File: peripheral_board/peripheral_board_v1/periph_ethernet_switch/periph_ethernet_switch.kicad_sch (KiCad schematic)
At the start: 57 parts, among them SW1 SW_DIP_x07, U1 KSZ9896CTXI, U2 25 MHz

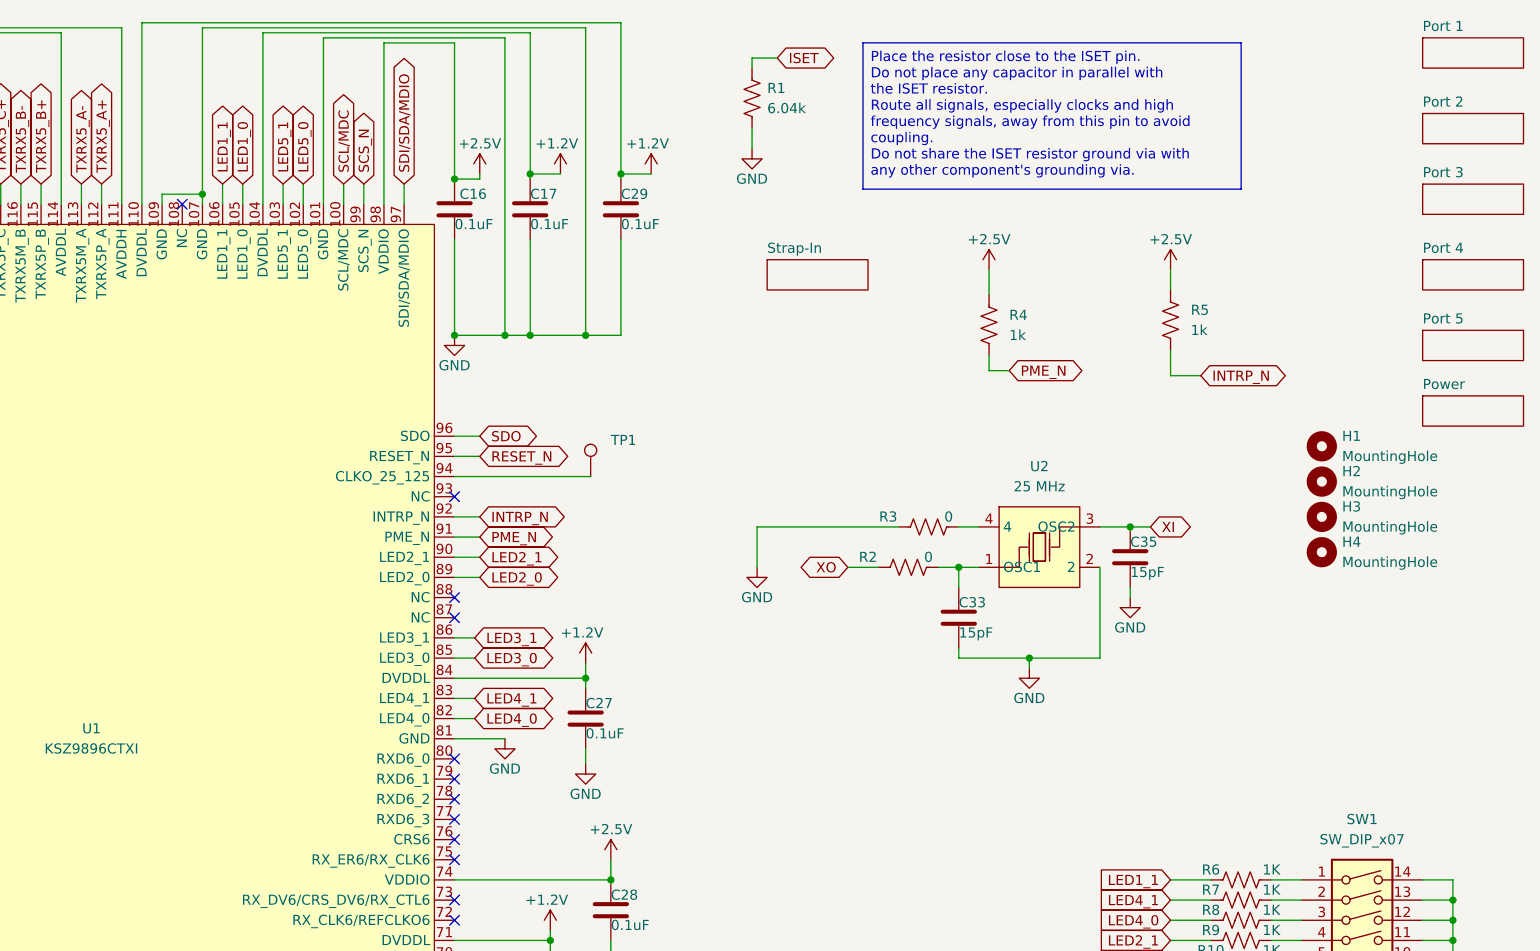
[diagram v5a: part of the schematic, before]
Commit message: Next version of the Switch
Got some feed back from Microchip. I sent it off for them look at. Will continue to make changes and updates here
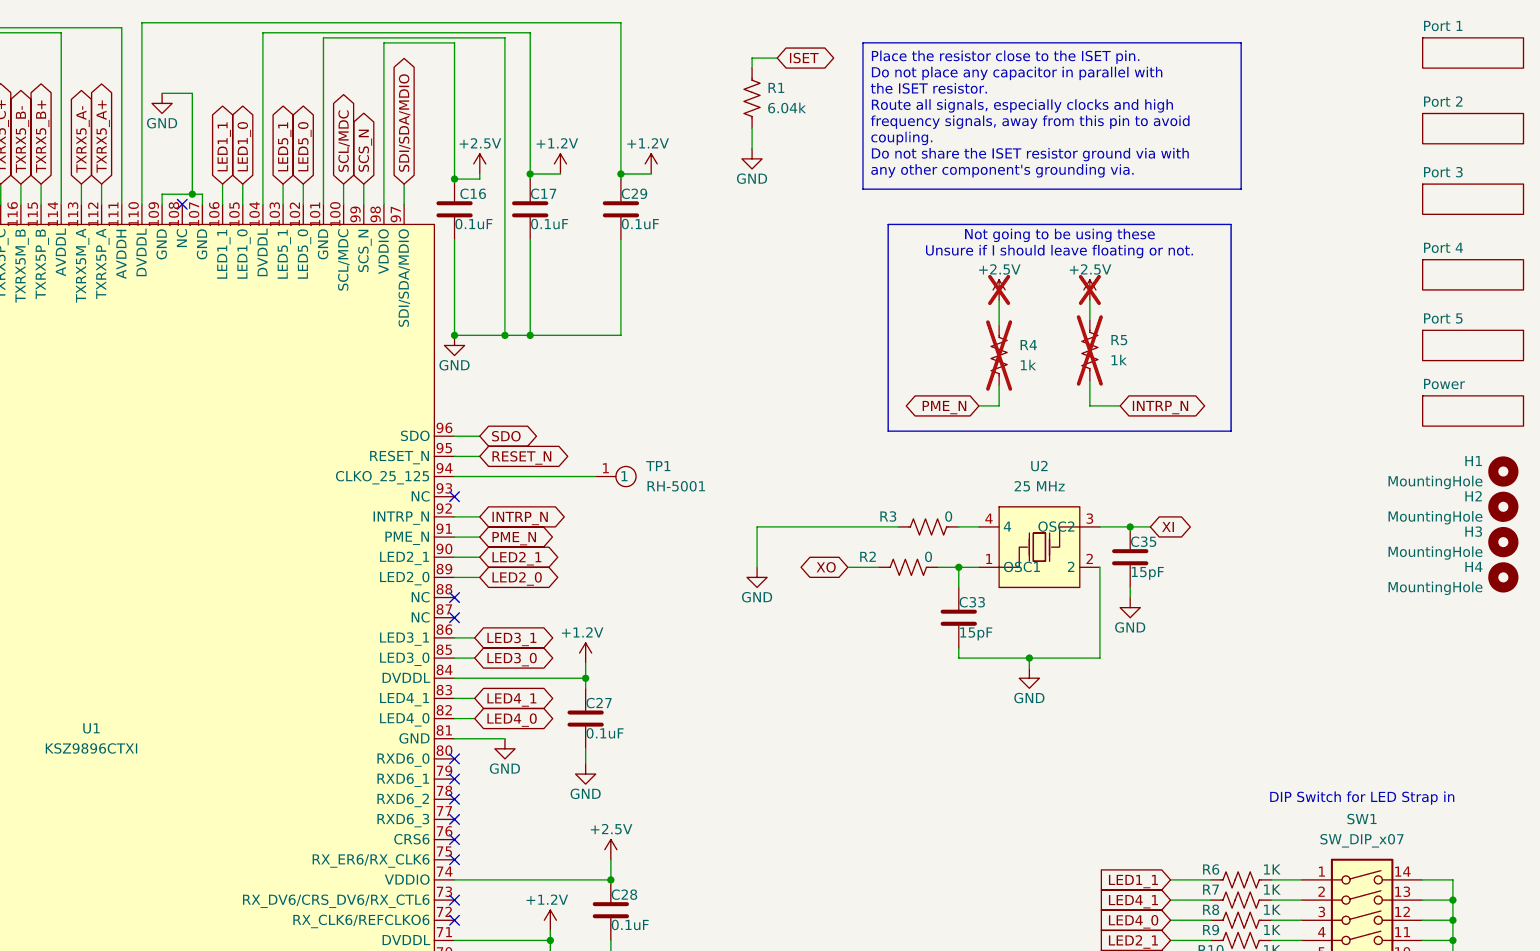
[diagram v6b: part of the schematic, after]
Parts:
- removed TP1: TestPoint, TestPoint:TestPoint_Pad_1.0x1.0mm, symbol Connector:TestPoint
- added TP1: RH-5001, SCALES:TEST-TH_BD2.54-P1.4_BLACK, symbol SCALES:RH-5001
- R4, R5: now not fitted; now left out of the parts list
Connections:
- net at U1.94 (CLKO_25_125): now also TP1.1
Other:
- removed sheet Strap-In
- note added: "DIP Switch for LED Strap in"
- note added: "Not going to be using these Unsure if I should leave floating or not."
- moved on the sheet: H1, H2, H3, H4

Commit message: Little changes to the PCB
Made a little bit of some changes of the traces for the decoupling caps.
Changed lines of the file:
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@@
 	)
 	(junction
-		(at 149.86 52.07)
-		(diameter 0)
-		(color 0 0 0 0)
-	)
-	(junction
 		(at 31.115 130.81)
 		(diameter 0)
@@
 	)
 	(junction
+		(at 170.18 52.07)
+		(diameter 0)
+		(color 0 0 0 0)
+	)
+	(junction
 		(at 154.305 151.13)
 		(diameter 0)
@@
 	(wire
 		(pts
-			(xy 159.385 52.07) (xy 170.815 52.07)
-		)
-		(stroke
-			(width 0)
-			(type default)
-		)
-	)
-	(wire
-		(pts
 			(xy 55.245 57.15) (xy 58.42 57.15)
 		)
@@
 	(wire
 		(pts
+			(xy 156.21 52.07) (xy 149.86 52.07)
+		)
+		(stroke
+			(width 0)
+			(type default)
+		)
+	)
+	(wire
+		(pts
 			(xy 271.78 135.89) (xy 275.59 135.89)
 		)
@@
 	(wire
 		(pts
+			(xy 170.18 54.61) (xy 170.18 52.07)
+		)
+		(stroke
+			(width 0)
+			(type default)
+		)
+	)
+	(wire
+		(pts
 			(xy 218.44 58.42) (xy 218.44 60.96)
 		)
@@
 	(wire
 		(pts
+			(xy 170.18 52.07) (xy 170.815 52.07)
+		)
+		(stroke
+			(width 0)
+			(type default)
+		)
+	)
+	(wire
+		(pts
 			(xy 55.245 34.925) (xy 64.77 34.925)
 		)
@@
 	(wire
 		(pts
-			(xy 149.86 52.07) (xy 156.21 52.07)
-		)
-		(stroke
-			(width 0)
-			(type default)
-		)
-	)
-	(wire
-		(pts
 			(xy 55.245 115.57) (xy 58.42 115.57)
 		)
@@
 	(wire
 		(pts
+			(xy 170.18 52.07) (xy 159.385 52.07)
+		)
+		(stroke
+			(width 0)
+			(type default)
+		)
+	)
+	(wire
+		(pts
 			(xy 220.345 153.67) (xy 220.345 155.575)
 		)
@@
 	(symbol
 		(lib_id "power:GND")
-		(at 149.86 52.07 0)
+		(at 170.18 54.61 0)
 		(unit 1)
 		(exclude_from_sim no)
@@
 		(dnp no)
 		(property "Reference" "#PWR026"
-			(at 149.86 58.42 0)
+			(at 170.18 60.96 0)
 			(effects
 				(font
@@
 		)
 		(property "Value" "GND"
-			(at 149.86 55.88 0)
+			(at 170.18 58.42 0)
 			(effects
 				(font
@@
 		)
 		(property "Footprint" ""
-			(at 149.86 52.07 0)
+			(at 170.18 54.61 0)
 			(effects
 				(font
@@
 		)
 		(property "Datasheet" ""
-			(at 149.86 52.07 0)
+			(at 170.18 54.61 0)
 			(effects
 				(font
@@
 		)
 		(property "Description" "Power symbol creates a global label with name \"GND\" , ground"
-			(at 149.86 52.07 0)
+			(at 170.18 54.61 0)
 			(effects
 				(font

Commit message: Updates from Microchip
Finally got a response for my schematic from Microchip support. Made a few changes that they recommended. Changed the crystal, updated a power pin, and added in the resistors for the LEDs. Sent it back with the updates and once it seems okay I will move everything over to layout and then send it to them there. I will need to make it in Altium to make life easier since they do not use KiCad.
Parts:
- removed R4, R5: 1k, Resistor_SMD:R_0603_1608Metric, symbol Device:R_US
- added C65, C66: 16pF, Capacitor_SMD:C_0603_1608Metric, symbol Device:C
- added TP10, TP11: RH-5001, SCALES:TEST-TH_BD2.54-P1.4_BLACK, symbol SCALES:RH-5001
- added Y1: MICROCHIP VXM7-9032-25M0000000, SCALES:CRYSTAL-SMD_4P-L3.2-W2.5-BL, symbol Device:Crystal_GND24
- C33, C35, R2, R3, U2: now not fitted; now left out of the parts list
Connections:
- net +2.5V: no longer C1.1, U1.111 (AVDDH)
- net +2.5VA: now also C1.1, U1.111 (AVDDH)
- net GND: now also C65.2, C66.2, Y1.2, Y1.4
- net INTRP_N: now also TP11.1
- net PME_N: now also TP10.1
- net XI: now also C66.1, Y1.3
- net XO: now also C65.1, Y1.1
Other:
- note added: "Clock"
- note added: "Left as a reference"
- note removed: "Not going to be using these Unsure if I should leave floating or not."
- moved on the sheet: C1
